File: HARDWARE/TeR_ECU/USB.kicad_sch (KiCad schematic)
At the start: 6 parts, among them J6 USB_B_Micro, U9 ADUM4160

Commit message: Quick changes
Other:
- moved on the sheet: C28, C29, J6, R11, R30, U9

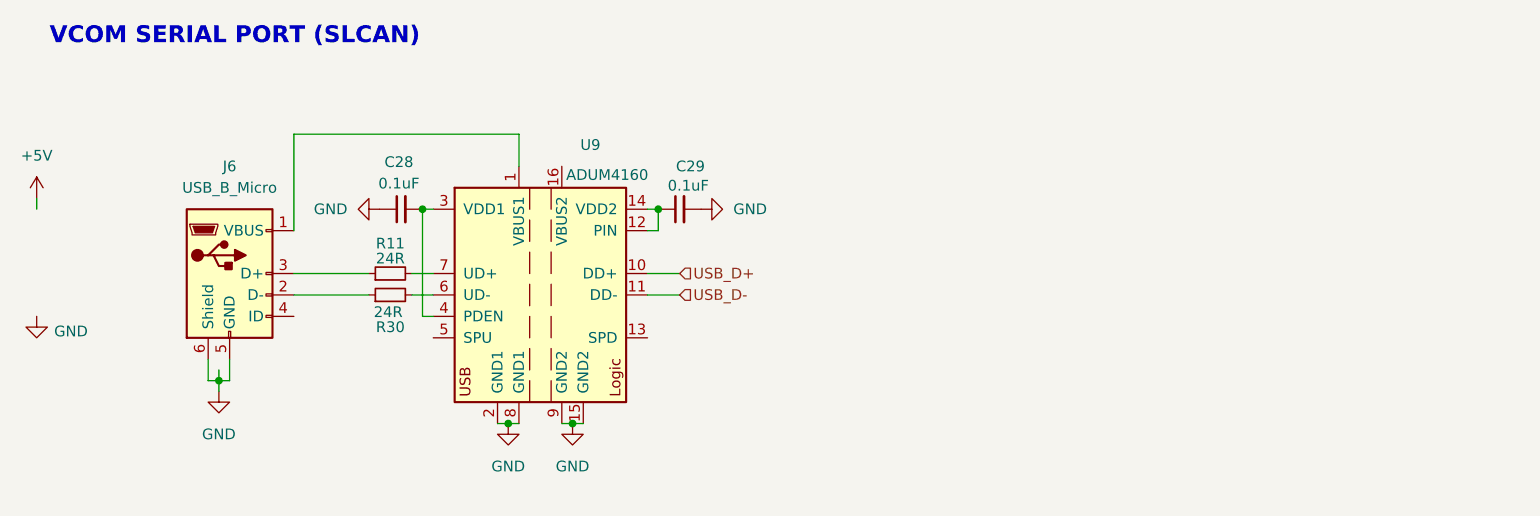
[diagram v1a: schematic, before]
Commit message: Advanced design and added IMU/GPS moduleç
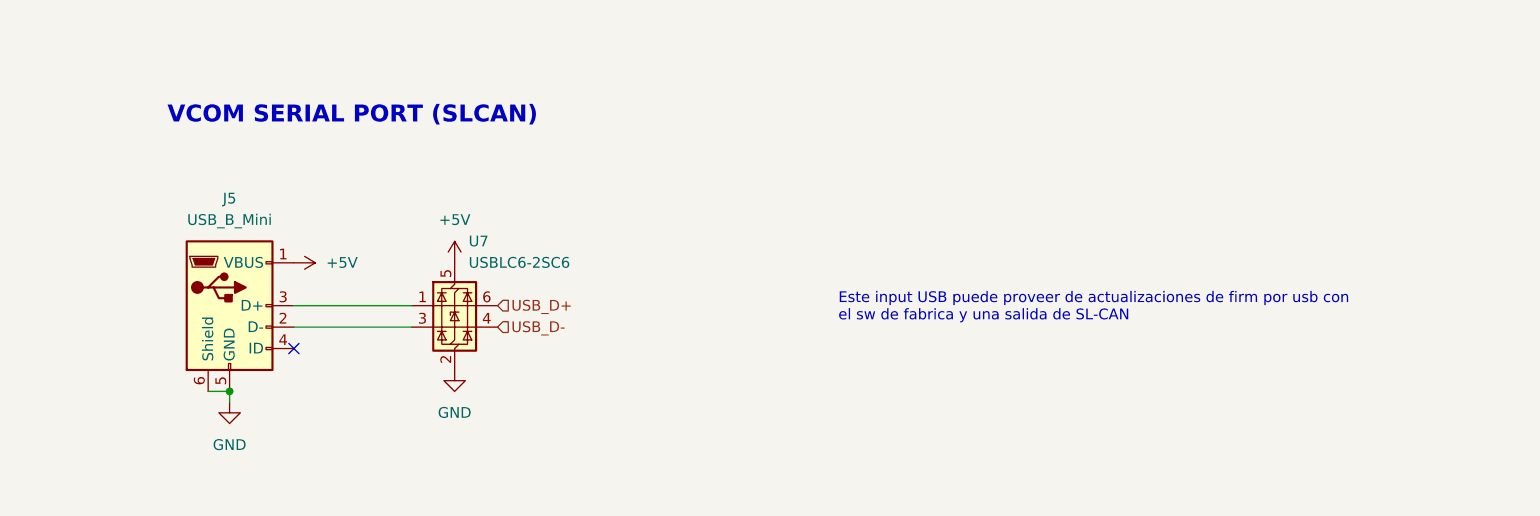
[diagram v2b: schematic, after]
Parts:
- removed C28, C29: 0.1uF, symbol Device:C_Small
- removed J6: USB_B_Micro, symbol Connector:USB_B_Micro
- removed R11, R30: 24R, symbol Device:R_Small
- removed U9: ADUM4160, Package_SO:SOIC-16W_7.5x10.3mm_P1.27mm, symbol Interface_USB:ADUM4160
- added J5: USB_B_Mini, symbol Connector:USB_B_Mini
- added U7: USBLC6-2SC6, Package_TO_SOT_SMD:SOT-23-6, symbol Power_Protection:USBLC6-2SC6
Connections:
- net +5V: now also J5.1 (VBUS), U7.5 (VBUS)
- net GND: now also J5.5 (GND), J5.6 (Shield), U7.2 (GND)
- net USB_D+: now also U7.6 (I/O1)
- net USB_D-: now also U7.4 (I/O2)
- new net: J5.3 (D+), U7.1 (I/O1)
- new net: J5.2 (D-), U7.3 (I/O2)
- no-connect marks 0 -> 1
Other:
- note added: "Este input USB puede proveer de actualizaciones de firm por usb con el sw de fabrica y una salida de SL-CAN"

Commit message: Quick changes, go to start layouting
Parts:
- J4: renamed from J5; footprint (none) -> Connector_USB:USB_Mini-B_Wuerth_65100516121_Horizontal
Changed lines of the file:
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@@
 		(dnp no)
 		(fields_autoplaced yes)
-		(property "Reference" "#PWR085"
+		(property "Reference" "#PWR0105"
 			(at 140.97 93.98 0)
 			(effects
@@
 			(project ""
 				(path "/84413845-c4f3-4743-bcd2-a67649c90902/f4983e62-bb86-4f44-906d-788ec401c377"
-					(reference "#PWR085")
+					(reference "#PWR0105")
 					(unit 1)
 				)
@@
 		(dnp no)
 		(fields_autoplaced yes)
-		(property "Reference" "#PWR086"
+		(property "Reference" "#PWR0106"
 			(at 140.97 109.22 0)
 			(effects
@@
 			(project ""
 				(path "/84413845-c4f3-4743-bcd2-a67649c90902/f4983e62-bb86-4f44-906d-788ec401c377"
-					(reference "#PWR086")
+					(reference "#PWR0106")
 					(unit 1)
 				)
@@
 		(dnp no)
 		(fields_autoplaced yes)
-		(property "Reference" "#PWR087"
+		(property "Reference" "#PWR0103"
 			(at 114.3 113.03 0)
 			(effects
@@
 			(project ""
 				(path "/84413845-c4f3-4743-bcd2-a67649c90902/f4983e62-bb86-4f44-906d-788ec401c377"
-					(reference "#PWR087")
+					(reference "#PWR0103")
 					(unit 1)
 				)
@@
 		(dnp no)
 		(fields_autoplaced yes)
-		(property "Reference" "#PWR084"
+		(property "Reference" "#PWR0104"
 			(at 118.11 90.17 0)
 			(effects
@@
 			(project "TeR_ECU"
 				(path "/84413845-c4f3-4743-bcd2-a67649c90902/f4983e62-bb86-4f44-906d-788ec401c377"
-					(reference "#PWR084")
+					(reference "#PWR0104")
 					(unit 1)
 				)
@@
 		(dnp no)
 		(fields_autoplaced yes)
-		(property "Reference" "J5"
+		(property "Reference" "J4"
 			(at 114.3 82.55 0)
 			(effects
@@
 			)
 		)
-		(property "Footprint" ""
+		(property "Footprint" "Connector_USB:USB_Mini-B_Wuerth_65100516121_Horizontal"
 			(at 118.11 96.52 0)
 			(effects
@@
 			(project ""
 				(path "/84413845-c4f3-4743-bcd2-a67649c90902/f4983e62-bb86-4f44-906d-788ec401c377"
-					(reference "J5")
-					(unit 1)
-				)
+					(reference "J4")
+					(unit 1)
+				)

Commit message: First layout prototype
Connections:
- net USB_D+: now also U7.1 (I/O1); no longer U7.6 (I/O1)
- net USB_D-: now also U7.3 (I/O2); no longer U7.4 (I/O2)
- net D+: now reaches J4.3 (D+)
- net D+: now also U7.6 (I/O1); no longer U7.1 (I/O1)
- net D-: now reaches J4.2 (D-)
- net D-: now also U7.4 (I/O2); no longer U7.3 (I/O2)
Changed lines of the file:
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@@
+		)
+	)
+	(label "D+"
+		(at 128.27 95.25 0)
+		(fields_autoplaced yes)
+		(effects
+			(font
+				(size 1.27 1.27)
+			)
+			(justify left bottom)
+		)
+	)
+	(label "D-"
+		(at 128.27 97.79 0)
+		(fields_autoplaced yes)
+		(effects
+			(font
+				(size 1.27 1.27)
+			)
+			(justify left bottom)
 		)
 	)
@@
 			)
 			(justify left)
-		)
-	)
-	(symbol
-		(lib_id "Power_Protection:USBLC6-2SC6")
-		(at 140.97 95.25 0)
-		(unit 1)
-		(exclude_from_sim no)
-		(in_bom yes)
-		(on_board yes)
-		(dnp no)
-		(fields_autoplaced yes)
-		(property "Reference" "U7"
-			(at 142.6211 87.63 0)
-			(effects
-				(font
-					(size 1.27 1.27)
-				)
-				(justify left)
-			)
-		)
-		(property "Value" "USBLC6-2SC6"
-			(at 142.6211 90.17 0)
-			(effects
-				(font
-					(size 1.27 1.27)
-				)
-				(justify left)
-			)
-		)
-		(property "Footprint" "Package_TO_SOT_SMD:SOT-23-6"
-			(at 142.24 101.6 0)
-			(effects
-				(font
-					(size 1.27 1.27)
-					(italic yes)
-				)
-				(justify left)
-				(hide yes)
-			)
-		)
-		(property "Datasheet" "https://www.st.com/resource/en/datasheet/usblc6-2.pdf"
-			(at 142.24 103.505 0)
-			(effects
-				(font
-					(size 1.27 1.27)
-				)
-				(justify left)
-				(hide yes)
-			)
-		)
-		(property "Description" "Very low capacitance ESD protection diode, 2 data-line, SOT-23-6"
-			(at 140.97 95.25 0)
-			(effects
-				(font
-					(size 1.27 1.27)
-				)
-				(hide yes)
-			)
-		)
-		(pin "3"
-		)
-		(pin "5"
-		)
-		(pin "6"
-		)
-		(pin "2"
-		)
-		(pin "4"
-		)
-		(pin "1"
-		)
-		(instances
-			(project ""
-				(path "/84413845-c4f3-4743-bcd2-a67649c90902/f4983e62-bb86-4f44-906d-788ec401c377"
-					(reference "U7")
-					(unit 1)
-				)
-			)
 		)
 	)
@@
 					(unit 1)
 				)
+			)
+		)
+	)
+	(symbol
+		(lib_id "Power_Protection:USBLC6-2SC6")
+		(at 140.97 95.25 0)
+		(mirror y)
+		(unit 1)
+		(exclude_from_sim no)
+		(in_bom yes)
+		(on_board yes)
+		(dnp no)
+		(property "Reference" "U7"
+			(at 139.3189 87.63 0)
+			(effects
+				(font
+					(size 1.27 1.27)
+				)
+				(justify left)
+			)
+		)
+		(property "Value" "USBLC6-2SC6"
+			(at 157.226 90.17 0)
+			(effects
+				(font
+					(size 1.27 1.27)
+				)
+				(justify left)
+			)
+		)
+		(property "Footprint" "Package_TO_SOT_SMD:SOT-23-6"
+			(at 139.7 101.6 0)
+			(effects
+				(font
+					(size 1.27 1.27)
+					(italic yes)
+				)
+				(justify left)
+				(hide yes)
+			)
+		)
+		(property "Datasheet" "https://www.st.com/resource/en/datasheet/usblc6-2.pdf"
+			(at 139.7 103.505 0)
+			(effects
+				(font
+					(size 1.27 1.27)
+				)
+				(justify left)
+				(hide yes)
+			)
+		)
+		(property "Description" "Very low capacitance ESD protection diode, 2 data-line, SOT-23-6"
+			(at 140.97 95.25 0)
+			(effects
+				(font
+					(size 1.27 1.27)
+				)
+				(hide yes)
+			)
+		)
+		(pin "3"
+		)
+		(pin "5"
+		)
+		(pin "6"
+		)
+		(pin "2"
+		)
+		(pin "4"
+		)
+		(pin "1"
+		)
+		(instances
+			(project "TeR_ECU"
+				(path "/84413845-c4f3-4743-bcd2-a67649c90902/f4983e62-bb86-4f44-906d-788ec401c377"
+					(reference "U7")
+					(unit 1)
+				)

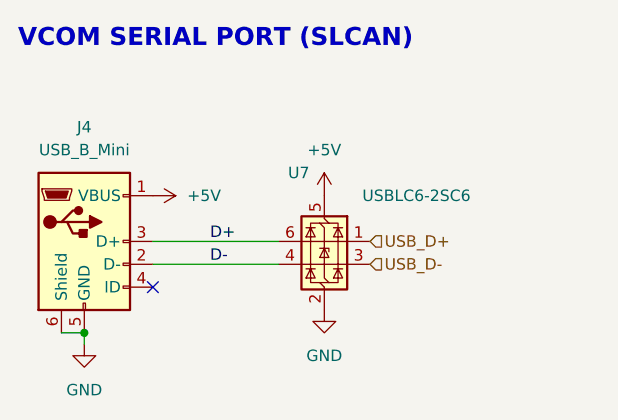
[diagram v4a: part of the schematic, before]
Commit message: Added Diode to clamp usb pwr
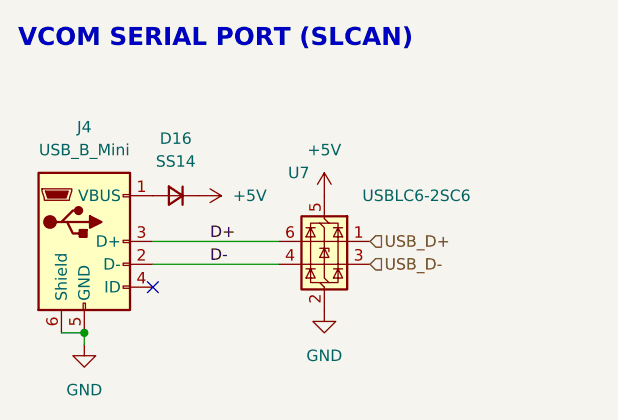
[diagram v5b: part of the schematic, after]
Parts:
- added D16: SS14, Diode_SMD:D_SOD-123, symbol Device:D_Small
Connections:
- net +5V: now also D16.1 (K); no longer J4.1 (VBUS)
- new net: D16.2 (A), J4.1 (VBUS)
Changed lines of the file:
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@@
+	)
+	(symbol
+		(lib_id "Device:D_Small")
+		(at 124.46 90.17 180)
+		(unit 1)
+		(exclude_from_sim no)
+		(in_bom yes)
+		(on_board yes)
+		(dnp no)
+		(fields_autoplaced yes)
+		(property "Reference" "D16"
+			(at 124.46 83.82 0)
+			(effects
+				(font
+					(size 1.27 1.27)
+				)
+			)
+		)
+		(property "Value" "SS14"
+			(at 124.46 86.36 0)
+			(effects
+				(font
+					(size 1.27 1.27)
+				)
+			)
+		)
+		(property "Footprint" "Diode_SMD:D_SOD-123"
+			(at 124.46 90.17 90)
+			(effects
+				(font
+					(size 1.27 1.27)
+				)
+				(hide yes)
+			)
+		)
+		(property "Datasheet" "~"
+			(at 124.46 90.17 90)
+			(effects
+				(font
+					(size 1.27 1.27)
+				)
+				(hide yes)
+			)
+		)
+		(property "Description" "Diode, small symbol"
+			(at 124.46 90.17 0)
+			(effects
+				(font
+					(size 1.27 1.27)
+				)
+				(hide yes)
+			)
+		)
+		(property "Sim.Device" "D"
+			(at 124.46 90.17 0)
+			(effects
+				(font
+					(size 1.27 1.27)
+				)
+				(hide yes)
+			)
+		)
+		(property "Sim.Pins" "1=K 2=A"
+			(at 124.46 90.17 0)
+			(effects
+				(font
+					(size 1.27 1.27)
+				)
+				(hide yes)
+			)
+		)
+		(pin "2"
+		)
+		(pin "1"
+		)
+		(instances
+			(project ""
+				(path "/84413845-c4f3-4743-bcd2-a67649c90902/f4983e62-bb86-4f44-906d-788ec401c377"
+					(reference "D16")
+					(unit 1)
+				)
+			)
+		)
 	)
 	(symbol
@@
 	(symbol
 		(lib_id "power:+5V")
-		(at 121.92 90.17 270)
+		(at 127 90.17 270)
 		(unit 1)
 		(exclude_from_sim no)
@@
 		(fields_autoplaced yes)
 		(property "Reference" "#PWR0104"
-			(at 118.11 90.17 0)
+			(at 123.19 90.17 0)
 			(effects
 				(font
@@
 		)
 		(property "Value" "+5V"
-			(at 125.73 90.1699 90)
+			(at 130.81 90.1699 90)
 			(effects
 				(font
@@
 		)
 		(property "Footprint" ""
-			(at 121.92 90.17 0)
+			(at 127 90.17 0)
 			(effects
 				(font
@@
 		)
 		(property "Datasheet" ""
-			(at 121.92 90.17 0)
+			(at 127 90.17 0)
 			(effects
 				(font
@@
 		)
 		(property "Description" "Power symbol creates a global label with name \"+5V\""
-			(at 121.92 90.17 0)
-			(effects
-				(font
+			(at 127 90.17 0)
+			(effects
+				(font
